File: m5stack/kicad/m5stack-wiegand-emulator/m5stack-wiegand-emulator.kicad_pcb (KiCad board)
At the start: 2 copper layers, 50 x 50 mm, 58 parts, among them J1 2x15 socket header, J2 2x15 pin header, J3 1x5 female, M1 M5 Stack 3.1mm mounting hole, M12 M5 Stack 1.1mm reference hole, M2 M5 Stack 3.1mm mounting hole, M3 M5 Stack 3.1mm mounting hole, M4 M5 Stack 3.1mm mounting hole, M5 M5 Stack 2mm mounting hole, M6 M5 Stack 2mm mounting hole, M7 M5 Stack 2mm mounting hole, M8 M5 Stack 2mm mounting hole, M9 M5 Stack 1.1mm reference hole, T1 TestPoint, T2 TestPoint, T3 TestPoint, T4 TestPoint, U1 RP2040, U2 ISOW7841, U3 SN74LVC2G126-EP, U6 FISM 1769405241

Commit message: M5: routing PCB
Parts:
- moved G*** 25.2 mm to (152.4, 92.7)
- moved D4 6.55 mm to (129.5, 87.6), turned to 180 degrees
- moved JP6 5.24 mm to (132.1, 72.4)
- moved R13 5.20 mm to (133.3, 92.4), turned to 90 degrees
- moved C1 3.81 mm to (129.5, 101.6)
- moved R12 3.81 mm to (129.5, 97.8)
- moved D1 2.58 mm to (135.9, 72.8)
- moved D3 2.09 mm to (129.5, 83.8), turned to 180 degrees
- moved D2 1.55 mm to (129.5, 81.3), turned to 180 degrees
- moved F1 1.27 mm to (114.3, 71.1)
- moved JP3 1.27 mm to (101.6, 92.7)
- moved JP1 1.27 mm to (101.6, 104.1)
- moved JP2 1.27 mm to (101.6, 99.1)
- moved T1 1.27 mm to (114.3, 66.0)
- moved T2 1.27 mm to (111.8, 66.0)
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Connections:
- J3 pad 1: /12VDC -> /LED
- J3 pad 2: GND -> /DO
- J3 pad 4: /DO -> GND
- J3 pad 5: /LED -> /12VDC
- JP6 pad 1: /12VDC -> Net-(D1-A)
- JP6 pad 2: Net-(D1-A) -> /12VDC
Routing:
- net GND: track 0.00 -> 72.2 mm, vias 0 -> 5
- net Net-(D1-K): track 0.00 -> 27.0 mm
- net +VDC: track 0.00 -> 15.2 mm
- net Net-(JP1-B): track 0.00 -> 14.2 mm
- net /LED: track 0.00 -> 10.0 mm
- net Net-(D5-COM): track 0.00 -> 8.28 mm
- net +5V: track 0.00 -> 7.93 mm
- net /12VDC: track 0.00 -> 7.13 mm
- net Net-(D1-A): track 0.00 -> 4.69 mm
- net /DI: track 0.00 -> 3.96 mm
- net Net-(U2-IND): track 0.00 -> 3.83 mm
- net /5VDC: track 0.00 -> 3.81 mm, vias 0 -> 1
- net /DO: track 0.00 -> 3.44 mm
- net /TXD2: vias 0 -> 1
- net /TXD1: vias 0 -> 1
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
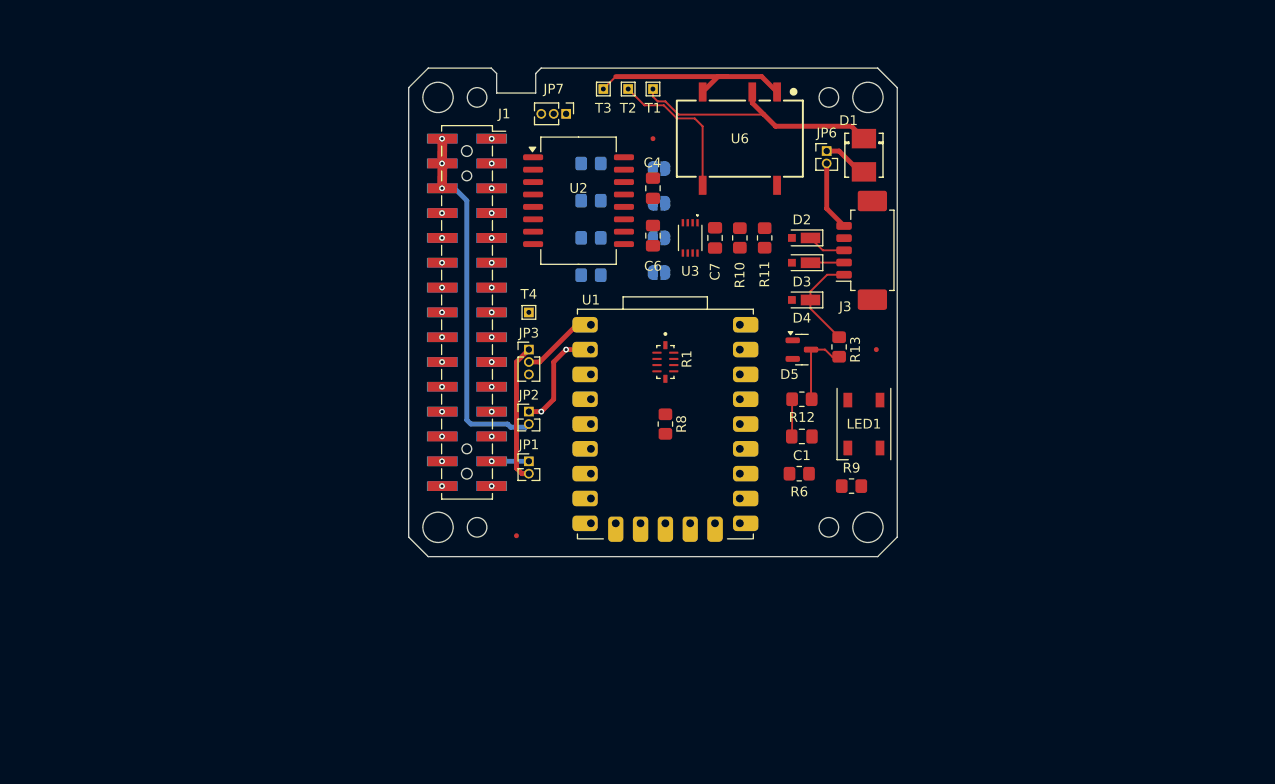
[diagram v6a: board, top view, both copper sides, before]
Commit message: Relocated J3 connector and rerouted
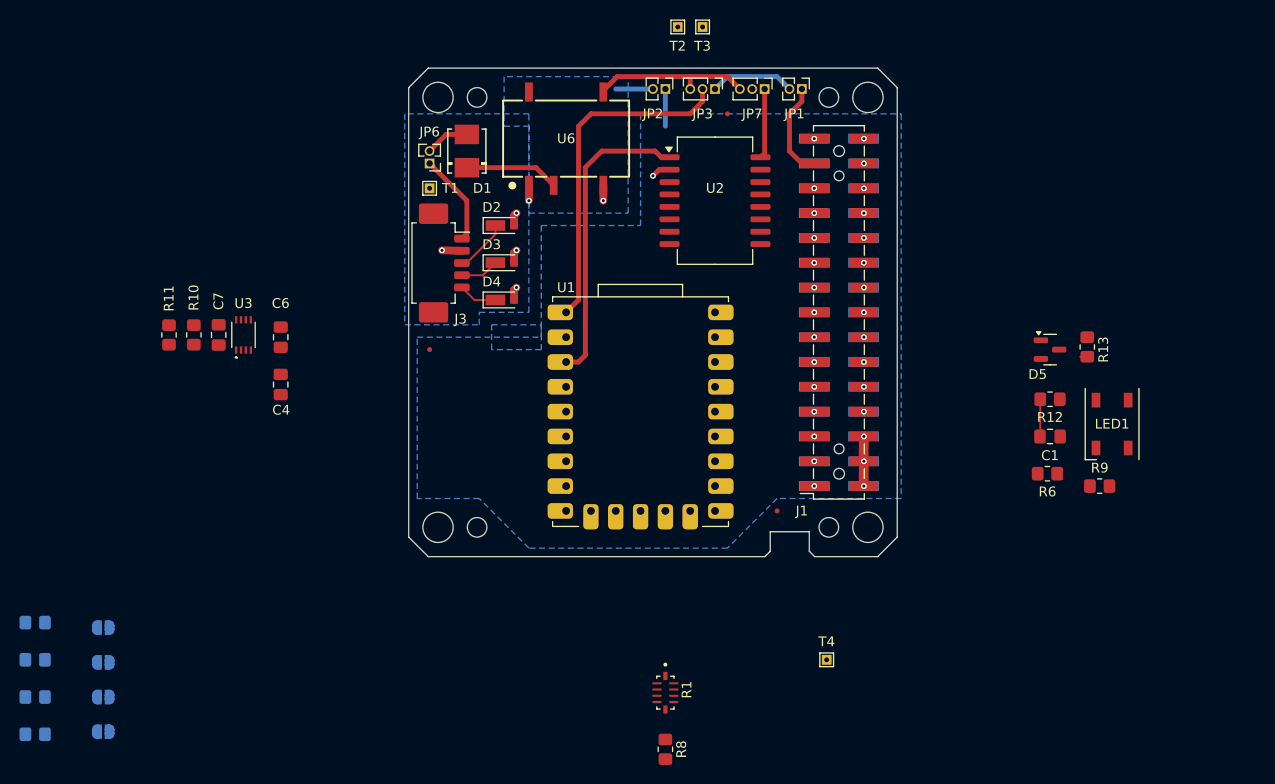
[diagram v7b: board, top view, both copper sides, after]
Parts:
- F1, F2, F3: value Fiducial_0.5mm_Mask1.5mm -> Fiducial_0.5mm_Mask1mm; footprint Fiducial:Fiducial_0.5mm_Mask1.5mm -> Fiducial:Fiducial_0.5mm_Mask1mm
- moved JP8 73.8 mm to (58.0, 128.3)
- moved R14 73.8 mm to (51.1, 120.7)
- moved R16 73.8 mm to (51.1, 128.3)
- moved R19 73.8 mm to (51.1, 132.1)
- moved JP4 73.8 mm to (58.0, 121.2)
- moved JP5 73.8 mm to (58.0, 124.7)
- moved JP9 73.8 mm to (58.0, 131.8)
- moved R15 73.8 mm to (51.1, 124.5)
- moved M1 62.2 mm to (136.3, 110.9), turned to 180 degrees
- moved M2 62.2 mm to (92.3, 110.9), turned to 180 degrees
- moved M3 62.2 mm to (92.3, 66.9), turned to 180 degrees
- moved M4 62.2 mm to (136.3, 66.9), turned to 180 degrees
- moved R11 61.8 mm to (64.8, 91.2), turned to -90 degrees
- moved M5 56.9 mm to (132.3, 110.9), turned to 180 degrees
- moved M6 56.9 mm to (96.3, 110.9), turned to 180 degrees
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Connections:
- C1 pad 2: GND -> GND1
- C6 pad 2: GND -> GND1
- C7 pad 2: GND -> GND1
- D2 pad 2: GND -> GND1
- D3 pad 2: GND -> GND1
- D4 pad 2: GND -> GND1
- D5 pad 1: GND -> GND1
- J3 pad 1: /LED -> /12VDC
- J3 pad 2: /DO -> GND1
- J3 pad 4: GND -> /DO
- J3 pad 5: /12VDC -> /LED
- JP2 pad 2: GND -> GND1
- JP6 pad 1: Net-(D1-A) -> /12VDC
- JP6 pad 2: /12VDC -> Net-(D1-A)
- LED1 pad 3: GND -> GND1
- R8 pad 2: GND -> GND1
- T3 pad 1: GND -> GND1
- U2 pad 15: GND -> GND1
- U2 pad 9: GND -> GND1
- U3 pad 4: GND -> GND1
- U6 pad 1: GND -> GND1
- U6 pad 4: GND -> GND1
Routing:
- net GND: track 72.2 -> 13.6 mm, vias 5 -> 4
- net +3V3: track 0.00 -> 31.0 mm
- net +5V: track 7.93 -> 34.6 mm
- net Net-(D1-K): track 27.0 -> 9.64 mm
- net GND1: track 0.00 -> 13.2 mm, vias 0 -> 6
- net Net-(D5-COM): track 8.28 -> 0.79 mm
- net VISO: track 0.00 -> 7.16 mm
- net /5VDC: track 3.81 -> 9.94 mm, vias 1 -> 0
- net /LED: track 10.0 -> 3.96 mm
- net Net-(JP1-B): track 14.2 -> 8.67 mm
- net /12VDC: track 7.13 -> 9.48 mm
- net /DI: track 3.96 -> 5.93 mm
- net +VDC: track 15.2 -> 16.5 mm
- net /DO: track 3.44 -> 4.35 mm
- added copper zone on B.Cu, net GND
- added copper zone on B.Cu, net GND1
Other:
- outline, holes or cut-outs redrawn

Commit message: M5: fixed (most) ERC violations
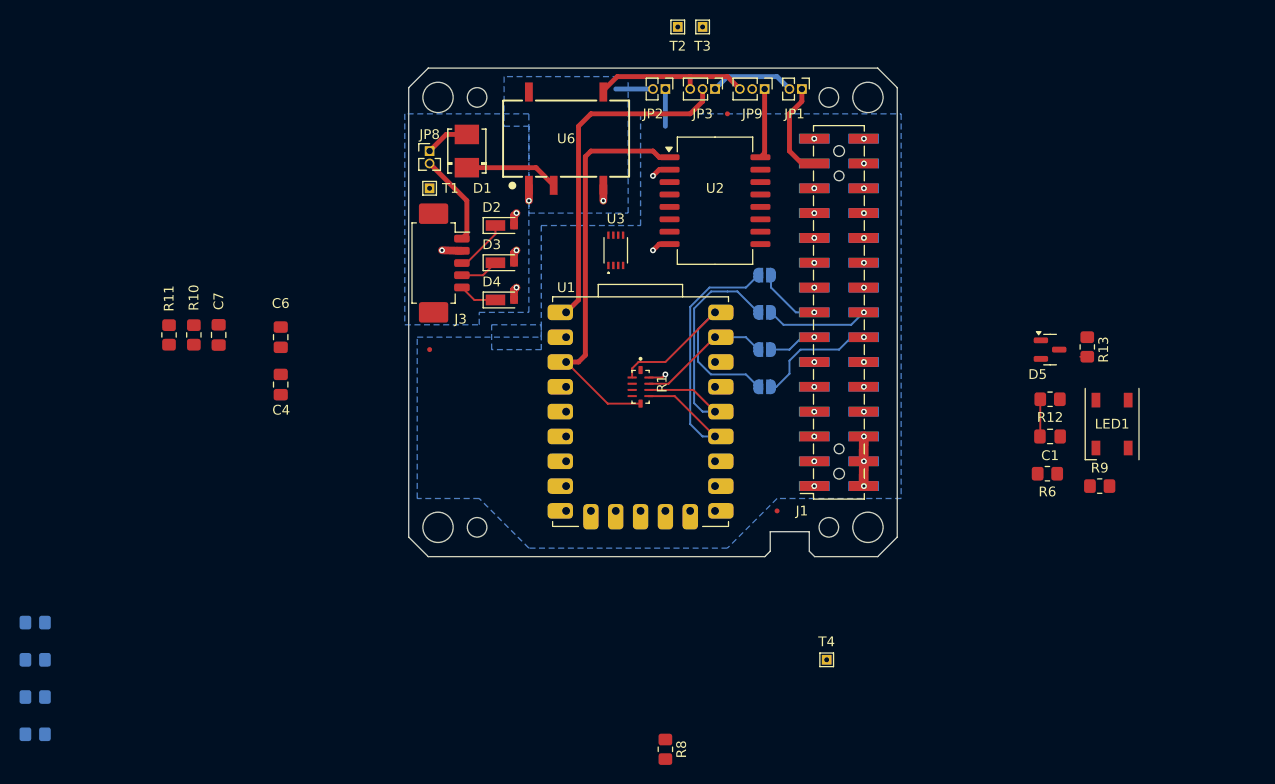
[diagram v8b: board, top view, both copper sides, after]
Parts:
- JP6: value Jumper_2_Bridged -> Jumper:SolderJumper_2_Open; footprint Connector_PinHeader_1.27mm:PinHeader_1x02_P1.27mm_Vertical -> Jumper:SolderJumper-2_P1.3mm_Open_RoundedPad1.0x1.5mm; moved to B.Cu
- JP7: value Jumper_3_Bridged12 -> Jumper:SolderJumper_2_Open; footprint Connector_PinHeader_1.27mm:PinHeader_1x03_P1.27mm_Vertical -> Jumper:SolderJumper-2_P1.3mm_Open_RoundedPad1.0x1.5mm; moved to B.Cu
- JP8: value Jumper:SolderJumper_2_Open -> Jumper; footprint Jumper:SolderJumper-2_P1.3mm_Open_RoundedPad1.0x1.5mm -> Connector_PinHeader_1.27mm:PinHeader_1x02_P1.27mm_Vertical; moved to F.Cu
- JP9: value Jumper:SolderJumper_2_Open -> Jumper_3_Bridged12; footprint Jumper:SolderJumper-2_P1.3mm_Open_RoundedPad1.0x1.5mm -> Connector_PinHeader_1.27mm:PinHeader_1x03_P1.27mm_Vertical; moved to F.Cu
- moved JP9 94.4 mm to (125.7, 66.0), turned to -90 degrees
- moved JP5 74.9 mm to (125.7, 92.7)
- moved JP4 72.0 mm to (125.7, 96.5)
- moved JP8 65.1 mm to (91.4, 72.4), turned to 0 degrees
- moved U3 39.1 mm to (110.5, 82.5)
- moved JP6 37.5 mm to (125.7, 88.9)
- moved R1 31.4 mm to (113.0, 96.5)
- moved JP7 19.0 mm to (125.7, 85.1), turned to 180 degrees
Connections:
- JP6 pad 1: /12VDC -> /RXD2
- JP6 pad 2: Net-(D1-A) -> Net-(JP6-B)
- JP7 pad 1: VISO -> /TXD2
- JP7 pad 2: Net-(JP7-C) -> Net-(JP7-B)
- JP8 pad 1: /RXD2 -> Net-(D1-A)
- JP8 pad 2: Net-(JP8-B) -> /12VDC
- JP9 pad 1: /TXD2 -> VISO
- JP9 pad 2: Net-(JP9-B) -> Net-(JP9-C)
- R1 pad 3: Net-(JP5-B) -> Net-(R1B-R2.2)
- R1 pad 4: Net-(JP8-B) -> Net-(R1C-R3.2)
- R1 pad 5: Net-(JP9-B) -> Net-(R1D-R4.2)
- R1 pad 7: Net-(R1E-R5.2) -> Net-(JP7-B)
- R1 pad 8: Net-(R1F-R6.2) -> Net-(JP6-B)
- R1 pad 9: Net-(R1G-R7.2) -> Net-(JP5-B)
- U1 pad 10: Net-(R1G-R7.2) -> Net-(R1B-R2.2)
- U1 pad 18: Net-(JP9-B) -> Net-(JP7-B)
- U1 pad 19: Net-(JP8-B) -> Net-(JP6-B)
- U1 pad 8: Net-(R1E-R5.2) -> Net-(R1D-R4.2)
- U1 pad 9: Net-(R1F-R6.2) -> Net-(R1C-R3.2)
- U2 pad 3: Net-(R1E-R5.2) -> Net-(R1D-R4.2)
- U2 pad 4: Net-(R1F-R6.2) -> Net-(R1C-R3.2)
- U2 pad 5: Net-(R1G-R7.2) -> Net-(R1B-R2.2)
- U3 pad 8: Net-(JP7-C) -> Net-(JP9-C)
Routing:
- net Net-(JP7-B): track 0.00 -> 31.8 mm
- net Net-(JP6-B): track 0.00 -> 28.0 mm
- net Net-(JP4-B): track 0.00 -> 24.8 mm
- net Net-(JP5-B): track 0.00 -> 13.7 mm
- net /RXD1: track 0.00 -> 12.4 mm
- net /RXD2: track 0.00 -> 10.5 mm
- net +3V3: track 31.0 -> 41.1 mm
- net /TXD2: track 0.00 -> 6.75 mm
- net /TXD1: track 0.00 -> 4.96 mm
- net GND: track 13.6 -> 17.3 mm, vias 4 -> 6
